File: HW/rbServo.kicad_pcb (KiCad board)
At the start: 4 copper layers, 19 x 32 mm, 37 parts, among them IC201 ATMEGA32M1_QFN32, P101 EXTCON, P104 p5V, P105 pGND, P109 pA, P113 M+, P114 M-, Q201 PMF170XP, U201 TJA1051, U202 LM3480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

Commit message: Trying new layout
Signed-off-by: RasmusB <RasmusB@users.noreply.github.com>
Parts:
- moved P104 28.6 mm to (190.0, 99.0)
- moved P109 28.2 mm to (192.0, 103.0)
- moved P105 27.4 mm to (191.0, 100.0)
- moved IC201 24.7 mm to (183.0, 104.0)
- moved ISP101 23.8 mm to (146.0, 97.0)
- moved C204 21.5 mm to (189.0, 112.0)
- moved Q201 19.9 mm to (163.8, 117.4), turned to 0 degrees
- moved C205 19.5 mm to (188.0, 112.0)
- moved C212 19.1 mm to (183.0, 96.0), turned to 0 degrees
- moved C210 18.7 mm to (174.0, 94.0)
- moved R209 18.6 mm to (183.0, 93.0)
- moved X201 18.0 mm to (183.0, 112.0)
- moved C209 17.9 mm to (139.0, 117.0)
- moved R206 17.9 mm to (139.0, 116.0)
- moved R207 17.9 mm to (139.0, 115.0)
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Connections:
- P101 pad 1: GND -> /Core/uIn
- P101 pad 2: /Core/CAN_HIGH -> /Core/CAN_LOW
- P101 pad 3: /Core/CAN_LOW -> /Core/CAN_HIGH
- P101 pad 4: /Core/uIn -> GND
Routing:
- net /Core/Isense: track 23.2 -> 0.00 mm, vias 4 -> 0
- net +BATT: track 20.9 -> 0.00 mm
- net +5V: track 15.9 -> 0.00 mm, vias 1 -> 0
- net GND: track 15.2 -> 0.00 mm, vias 6 -> 0
- net /Core/PWM_A: track 13.5 -> 0.00 mm, vias 2 -> 0
- net /Core/m_EN: track 9.64 -> 0.00 mm, vias 2 -> 0
- net /Core/CAN_HIGH: track 8.30 -> 0.00 mm, vias 1 -> 0
- net /Core/CAN_LOW: track 8.00 -> 0.00 mm, vias 1 -> 0
- net Net-(C205-Pad1): track 5.10 -> 0.00 mm
- net /Core/ISP_MISO: track 4.65 -> 0.00 mm
- net /Core/M+: track 4.45 -> 0.00 mm, vias 8 -> 0
- net /Core/ledB: track 3.99 -> 0.00 mm
- net /Core/ledA: track 3.65 -> 0.00 mm
- net /Core/uBattFB: track 3.02 -> 0.00 mm
- net Net-(C204-Pad1): track 2.98 -> 0.00 mm
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- removed copper zone on Inner2.Cu, net /Core/Isense
- removed copper zone on B.Cu, net /Core/M+
- removed copper zone on F.Cu, net /Core/M+
- removed copper zone on F.Cu, net /Core/M-
- removed copper zone on Inner1.Cu, net /Core/uIn
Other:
- board size 19 x 32 mm -> 17.8 x 28 mm

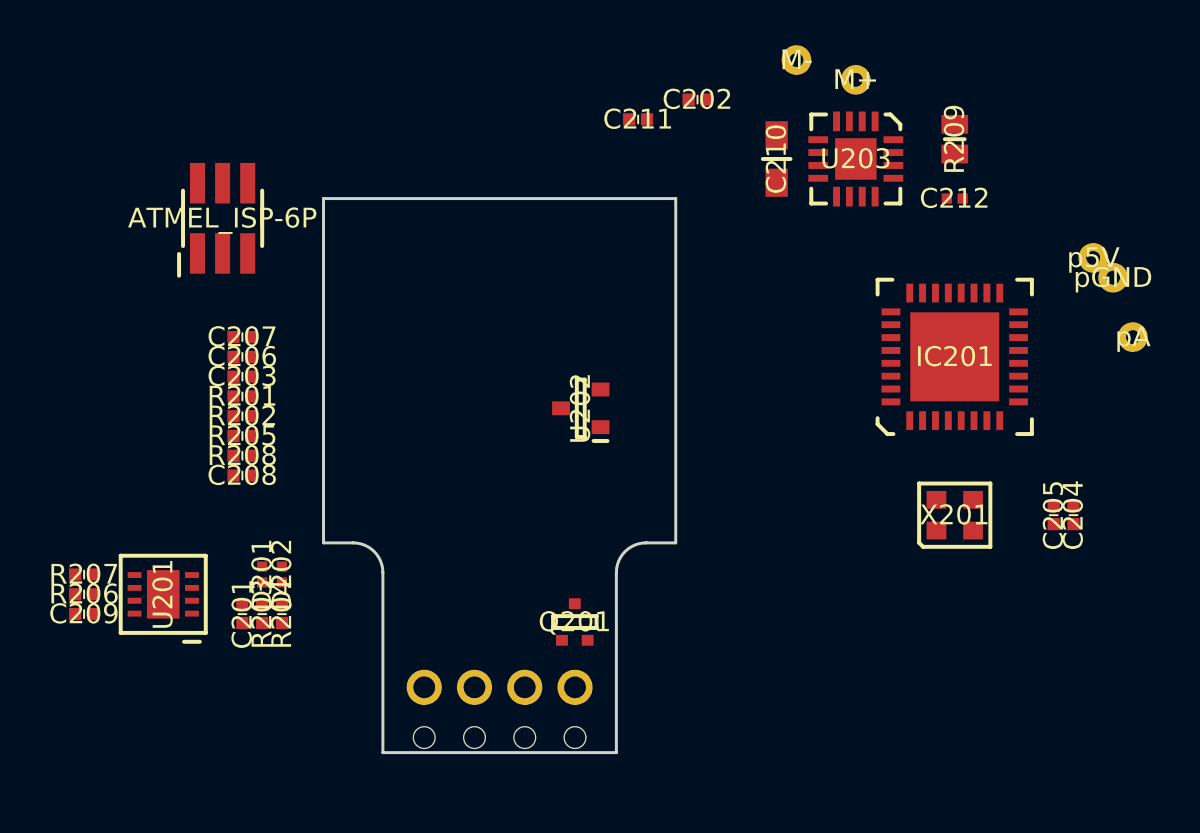
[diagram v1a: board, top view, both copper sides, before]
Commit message: -Swapped CAN_H and CAN_L -Changed a few labels - All new layout that should fit i a servo
Signed-off-by: RasmusB <RasmusB@users.noreply.github.com>
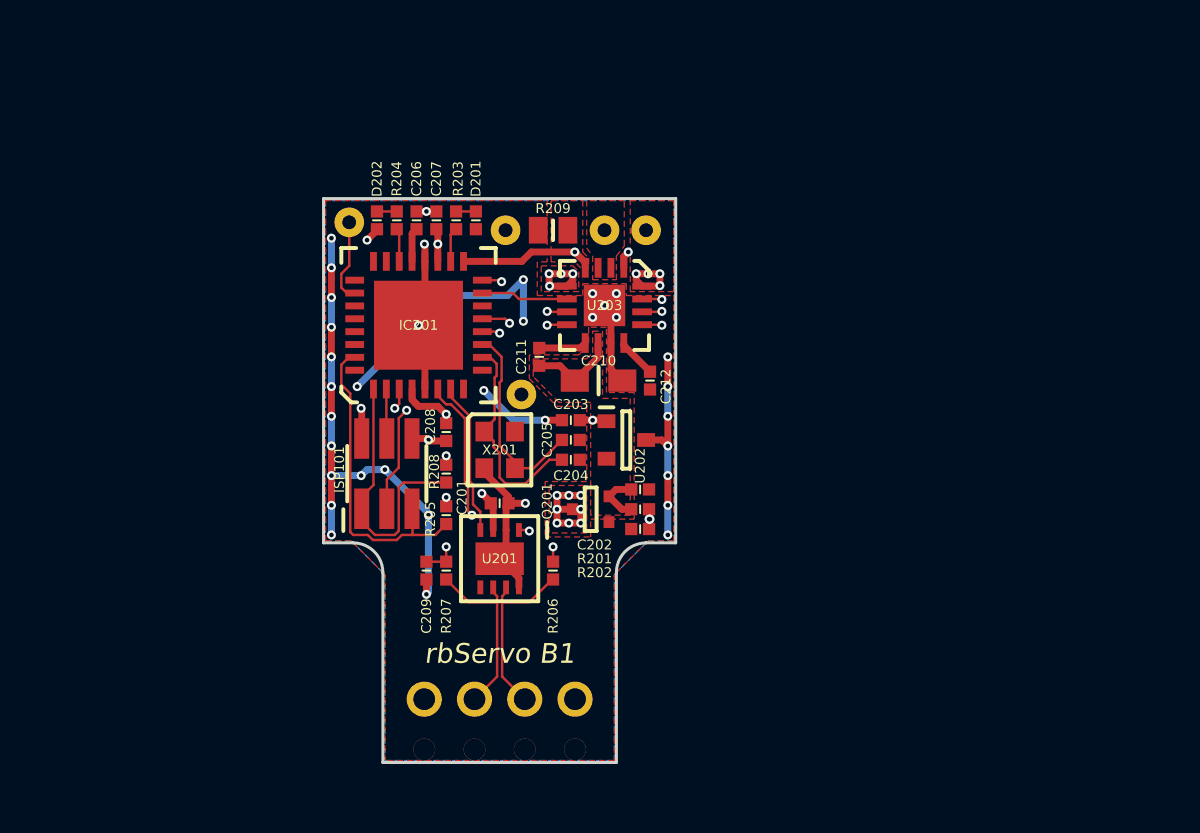
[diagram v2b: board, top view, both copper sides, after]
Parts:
- P101: footprint rbv_connectors:MPT_0,5%2f2,54x04 -> rbv_connectors:MPT_0,5_2,54x04
- P104: value p5V -> 5V; moved to B.Cu
- P105: value pGND -> GND; moved to B.Cu
- P109: value pA -> Pot; moved to B.Cu
- P113, P114: moved to B.Cu
- moved P109 40.0 mm to (152.4, 97.2)
- moved P105 30.8 mm to (160.3, 97.6)
- moved P104 29.7 mm to (161.1, 105.9)
- moved IC201 27.1 mm to (155.9, 102.4)
- moved C204 25.6 mm to (163.6, 109.2), turned to 0 degrees
- moved C205 24.7 mm to (163.6, 108.2), turned to 0 degrees
- moved R206 23.7 mm to (162.7, 114.8), turned to 90 degrees
- moved X201 23.2 mm to (160.0, 108.7), turned to 270 degrees
- moved R203 22.2 mm to (157.8, 97.1), turned to 90 degrees
- moved D201 20.9 mm to (158.8, 97.1)
- moved R201 20.9 mm to (167.1, 111.7)
- moved R202 20.9 mm to (167.1, 112.7)
- moved R209 20.8 mm to (162.7, 97.6), turned to 180 degrees
- moved R204 20.7 mm to (154.8, 97.1), turned to 90 degrees
- moved C202 19.9 mm to (167.1, 110.7)
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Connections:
- net Net-(C212-Pad1) renamed /Core/vInt
- D201 pad 1: /Core/ledA -> Net-(D201-Pad1)
- D201 pad 2: Net-(D201-Pad2) -> GND
- D202 pad 1: /Core/ledB -> Net-(D202-Pad1)
- D202 pad 2: Net-(D202-Pad2) -> GND
- IC201 pad 13: Net-(IC201-Pad13) -> /Core/uBattFB
- IC201 pad 15: /Core/m_EN -> /Core/m_FAULT
- IC201 pad 16: /Core/aPot -> /Core/m_EN
- IC201 pad 17: Net-(IC201-Pad17) -> /Core/Isense
- IC201 pad 18: Net-(IC201-Pad18) -> /Core/ledA
- IC201 pad 22: Net-(IC201-Pad22) -> /Core/ledB
- IC201 pad 26: /Core/Isense -> /Core/aPot
- IC201 pad 27: /Core/uBattFB -> Net-(IC201-Pad27)
- IC201 pad 8: /Core/ledA -> Net-(IC201-Pad8)
- IC201 pad 9: /Core/ledB -> Net-(IC201-Pad9)
- P101 pad 2: /Core/CAN_LOW -> /Core/CAN_HIGH
- P101 pad 3: /Core/CAN_HIGH -> /Core/CAN_LOW
- R203 pad 1: Net-(D201-Pad2) -> /Core/ledA
- R203 pad 2: GND -> Net-(D201-Pad1)
- R204 pad 1: Net-(D202-Pad2) -> /Core/ledB
- R204 pad 2: GND -> Net-(D202-Pad1)
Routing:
- net GND: track 0.00 -> 80.1 mm, vias 0 -> 38
- net /Core/PWM_B: track 0.00 -> 19.3 mm, vias 0 -> 3
- net /Core/PWM_A: track 0.00 -> 19.1 mm, vias 0 -> 3
- net /Core/ISP_RES: track 0.00 -> 16.2 mm
- net /Core/uBattFB: track 0.00 -> 15.4 mm, vias 0 -> 3
- net /Core/ISP_MISO: track 0.00 -> 13.9 mm
- net /Core/m_EN: track 0.00 -> 12.8 mm, vias 0 -> 2
- net /Core/ISP_SCK: track 0.00 -> 12.6 mm, vias 0 -> 2
- net /Core/CAN_TX: track 0.00 -> 11.0 mm, vias 0 -> 2
- net Net-(C204-Pad1): track 0.00 -> 11.0 mm
- net +5V: track 0.00 -> 10.5 mm, vias 0 -> 6
- net /Core/Isense: track 0.00 -> 10.4 mm, vias 0 -> 2
- net Net-(C205-Pad1): track 0.00 -> 10.2 mm
- net /Core/CAN_HIGH: track 0.00 -> 9.25 mm
- net /Core/CAN_LOW: track 0.00 -> 9.25 mm
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- added copper zone on Inner2.Cu, net +5V
- added copper zone on F.Cu, net +BATT
- added copper zone on F.Cu, net /Core/Isense
- added copper zone on F.Cu, net /Core/M+
- added copper zone on Inner2.Cu, net /Core/M+
- added copper zone on F.Cu, net /Core/M-
- added copper zone on F.Cu, net /Core/uIn
- added copper zone on Inner2.Cu, net /Core/uIn
- added copper zone on B.Cu, net GND
- added copper zone on F.Cu, net GND
- added copper zone on Inner1.Cu, net GND
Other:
- board size 17.8 x 28 mm -> 17.8 x 28.5 mm
- rule pad_to_mask_clearance: 0.07 -> 0
- board text added: "CAN_H"
- board text added: "CAN_L"
- board text added: "GND"
- board text added: "V+"
- board text added: "rbServo B1"
